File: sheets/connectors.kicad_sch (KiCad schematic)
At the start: 4 parts

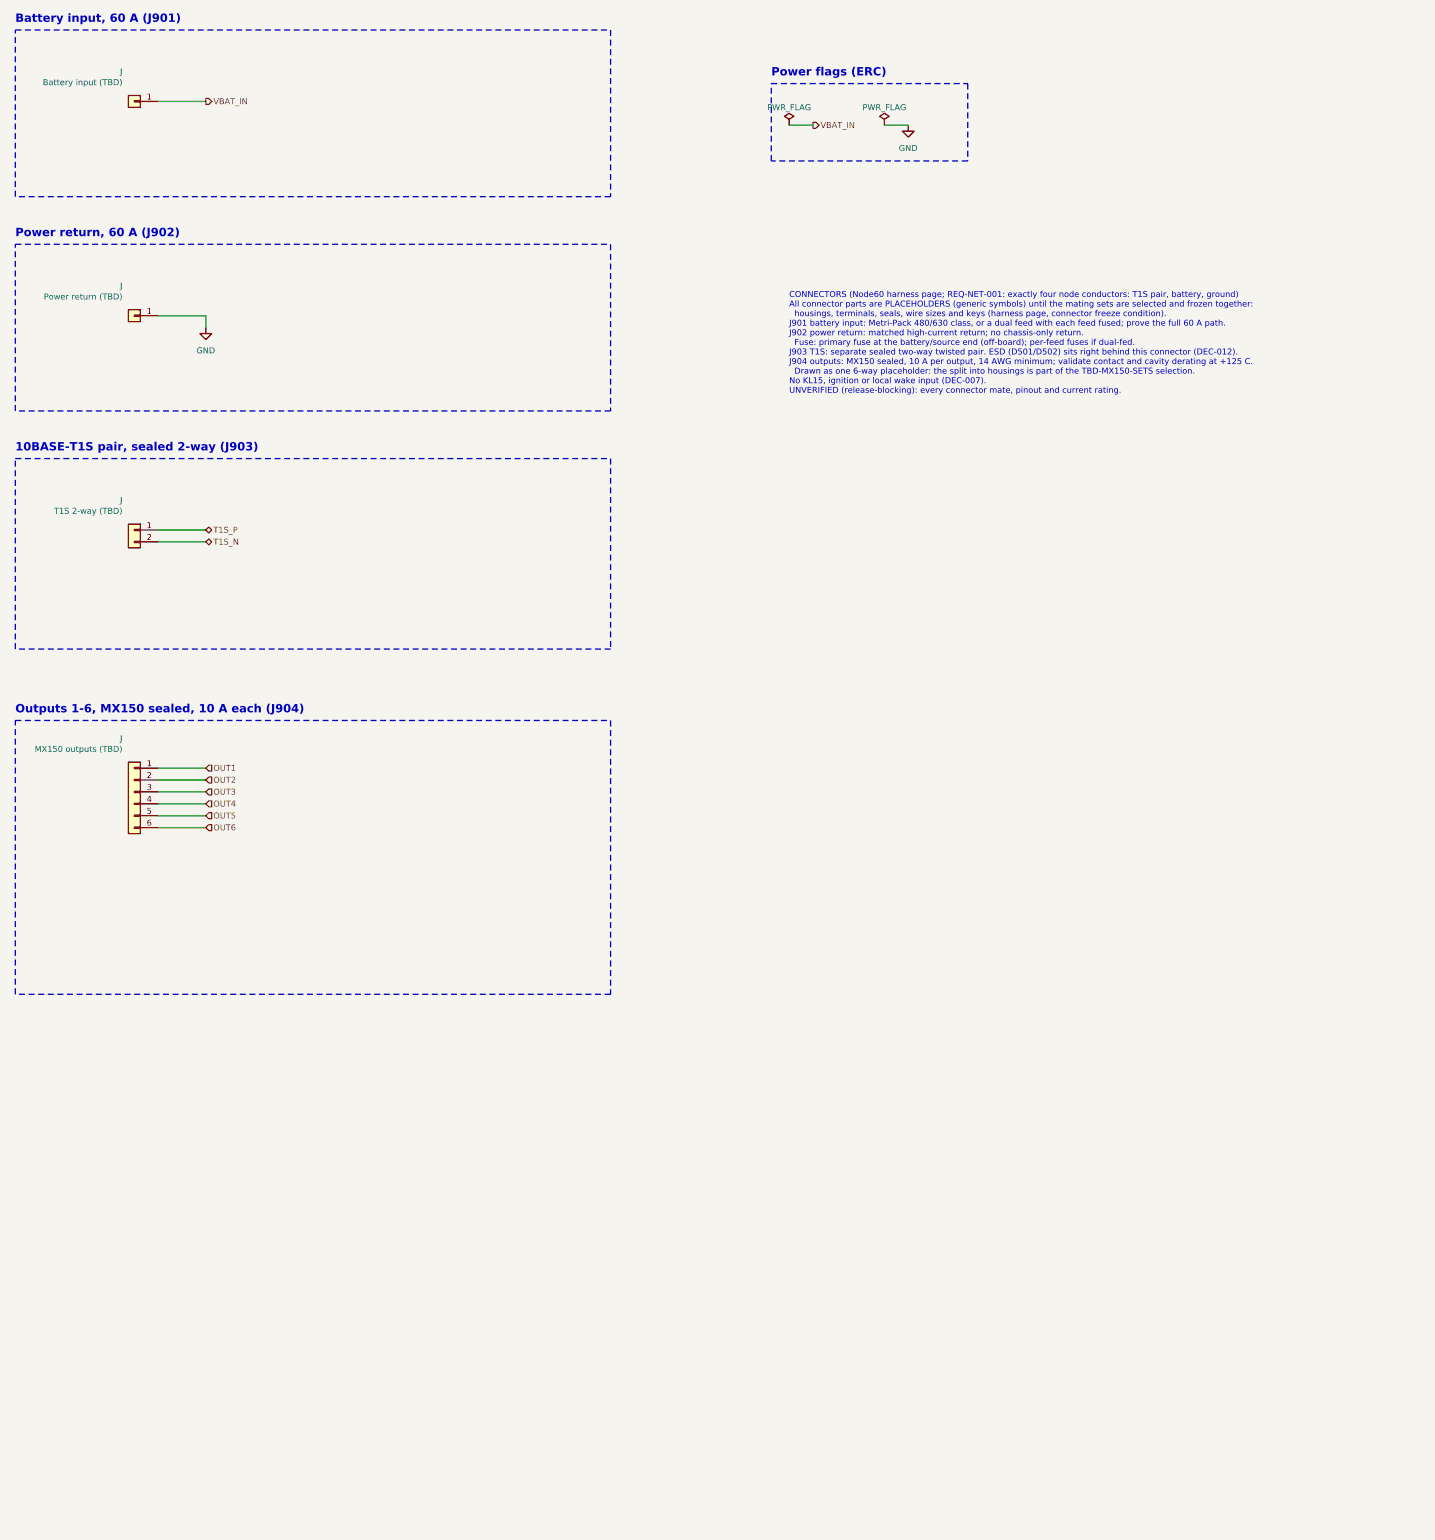
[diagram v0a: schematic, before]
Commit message: Connectors: six DT13-2P output headers replace the MX150 placeholder
J904-J909, one TE Deutsch DT13-2P per output (DEC-013, node60-hw PR #8).
Still placeholders until DropOut_Connector:DT13-2P lands (library PR
#19). Pin 1 carries OUTx; pin 2 stays unconnected with a visible note
until the pin assignment (local ground return vs paralleled output) is
decided.

Co-Authored-By: Claude Opus 5.5 <noreply@anthropic.com>
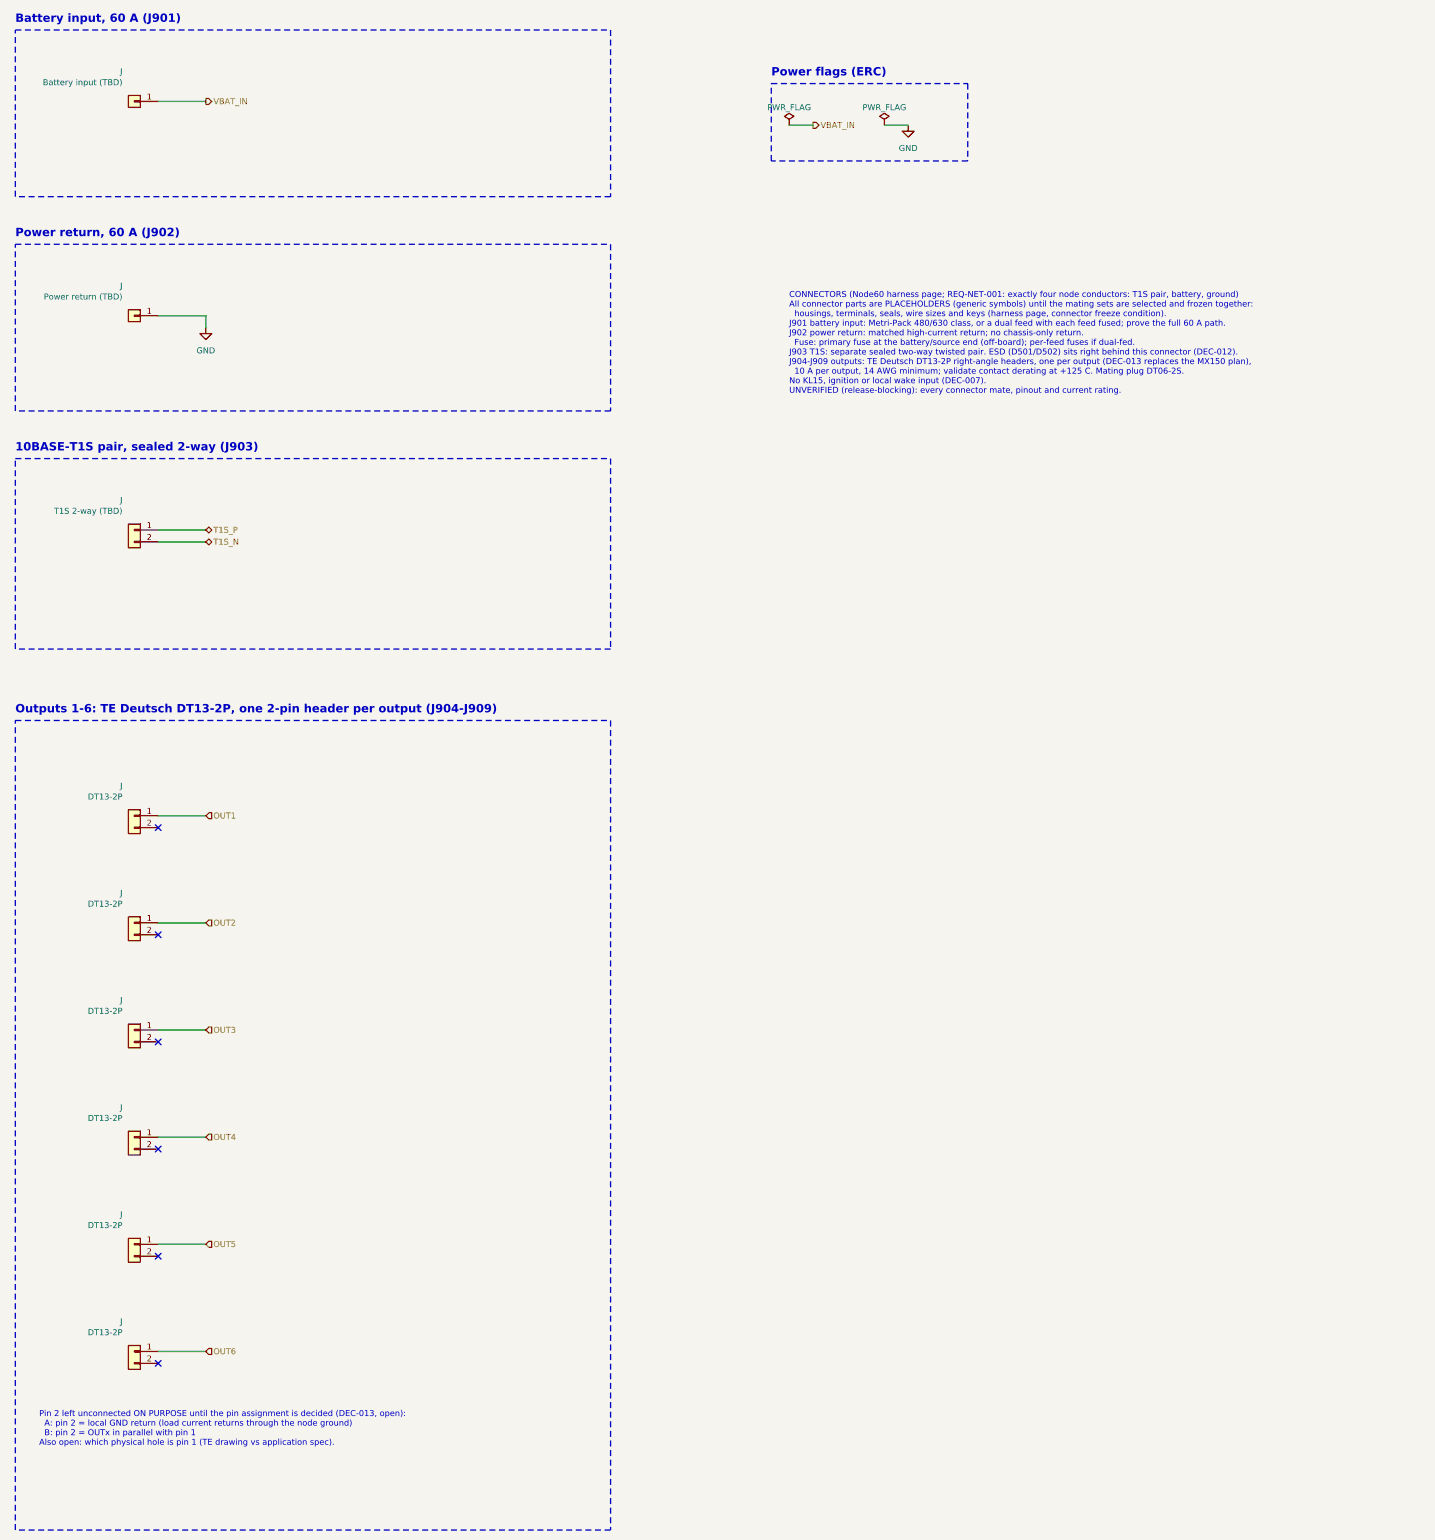
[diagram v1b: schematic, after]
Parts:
- added J (x5): DT13-2P, symbol Connector_Generic:Conn_01x02
- J: value MX150 outputs (TBD) -> DT13-2P; symbol Connector_Generic:Conn_01x06 -> Connector_Generic:Conn_01x02; Placeholder PLACEHOLDER: TBD part: selection pending user decision (fin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 -> PLACEHOLDER: selected 2026-10-23 (DEC-013): TE DT13-2P; lib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
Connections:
- net OUT2: now also J.1 (Pin_1); no longer J.2 (Pin_2)
- net OUT3: now also J.1 (Pin_1); no longer J.3 (Pin_3)
- net OUT4: now also J.1 (Pin_1); no longer J.4 (Pin_4)
- net OUT5: now also J.1 (Pin_1); no longer J.5 (Pin_5)
- net OUT6: now also J.1 (Pin_1); no longer J.6 (Pin_6)
- no-connect marks 0 -> 6
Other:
- note added: "Outputs 1-6: TE Deutsch DT13-2P, one 2-pin header per output (J904-J909)"
- note added: "Pin 2 left unconnected ON PURPOSE until the pin assignment is decided (DEC-013, open): A: pin 2 = local GND return (load current returns through the node ground) B: pin 2 = OUTx in parallel with pin 1 Also open: which physical hole is pin 1 (TE drawing vs application spec)."
- note removed: "Outputs 1-6, MX150 sealed, 10 A each (J904)"

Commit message: Connectors: DT13-2P pin 2 is the load ground return
Per DEC-013 (decided 2026-10-22, node60-hw PR #8): pin 1 = OUTx, pin 2 =
that load's ground return, on the single GND net. The sheet notes the
layout consequences: each return sized like its 10 A output and routed
to the power-entry star region, never across the logic ground, with up
to 60 A of load return leaving through J902.

Co-Authored-By: Claude Opus 5.5 <noreply@anthropic.com>
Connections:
- net GND: now also J.2 (Pin_2), J.2 (Pin_2), J.2 (Pin_2), J.2 (Pin_2), J.2 (Pin_2), J.2 (Pin_2)
- no-connect marks 6 -> 0
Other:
- note added: "Pin 1 = OUTx, pin 2 = that load's ground return (DEC-013, decided 2026-10-22). LAYOUT: each pin 2 return carries up to 10 A, like its OUTx: same copper and via treatment. Route pin 2 returns to the power-entry ground star region, never across the logic ground. Up to 60 A of load return flows from the headers to the star region and out through J902. RELEASE-BLOCKING: which physical hole is pin 1 (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"
- note removed: "Pin 2 left unconnected ON PURPOSE until the pin assignment is decided (DEC-013, open): A: pin 2 = local GND return (load current returns through the node ground) B: pin 2 = OUTx in parallel with pin 1 Also open: which physical hole is pin 1 (TE drawing vs application spec)."

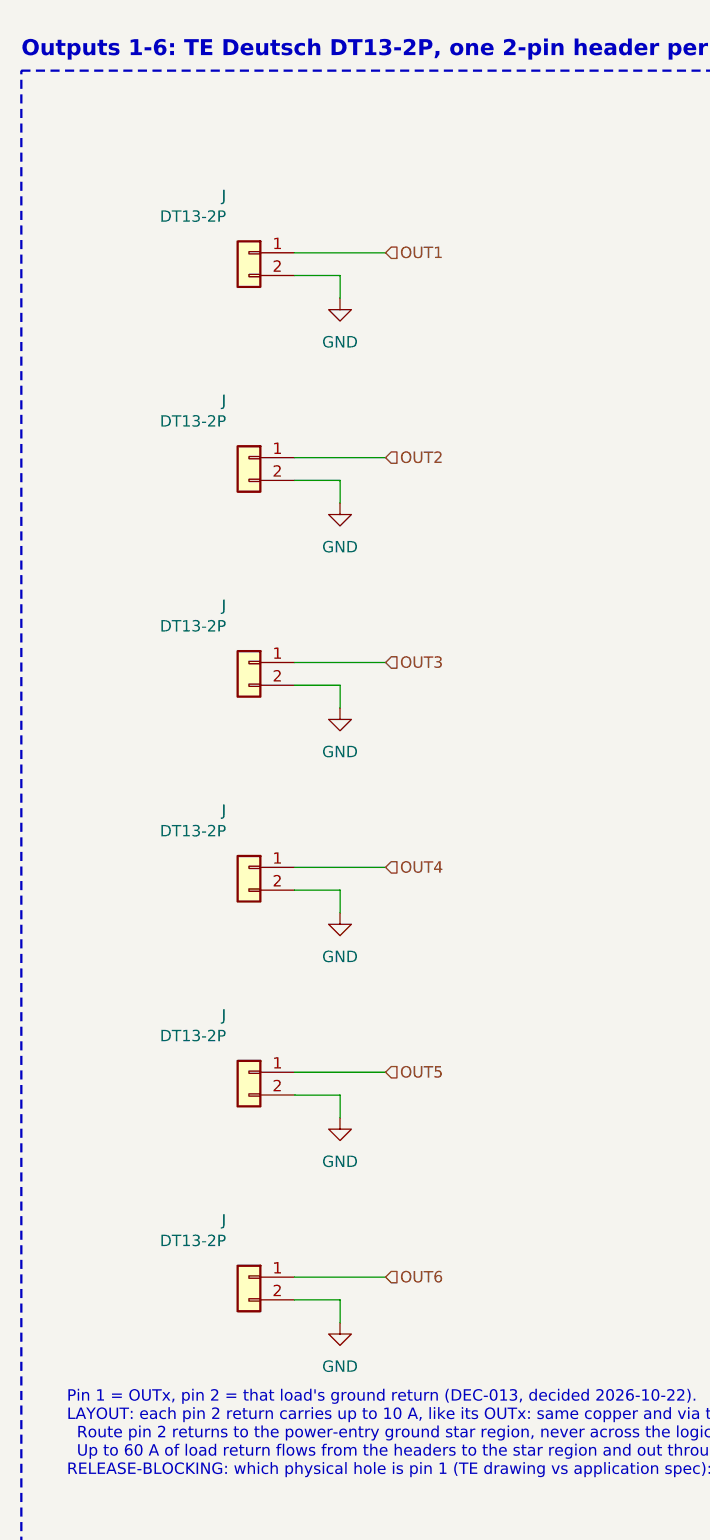
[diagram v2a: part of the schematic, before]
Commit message: Swap placeholders for merged DropOut library parts
Library bumped to ce98ecf (PRs #15, #16, #18, #19, #20, #21 merged).
Now real parts: IAUTN08S5N012LATMA1 (Q201-Q204, dual gate: G_ON and
G_LIN both driven), CSS2725FTL250 (R201, 2-terminal: sense nets are
VBAT_D / VBAT_Q2D with Kelvin taps from the pads in layout),
TPS7B8133QWDRVRQ1 (U301, COUT 2.2uF per its 1-200 uF requirement),
NCU18XH103F6SRB (RT201, RT601-801), Wurth 74438356022HT / 74438356010HT
buck inductors and Harwin S1751-46R GND loops (user's picks 2026-10-23),
1 mm pad test points and DT13-2P output headers. The library pin-type
fixes cut the ERC exclusions from 17 to 2. parts.yaml records the
library symbols; the library tables list the new libraries.

Co-Authored-By: Claude Opus 5.5 <noreply@anthropic.com>
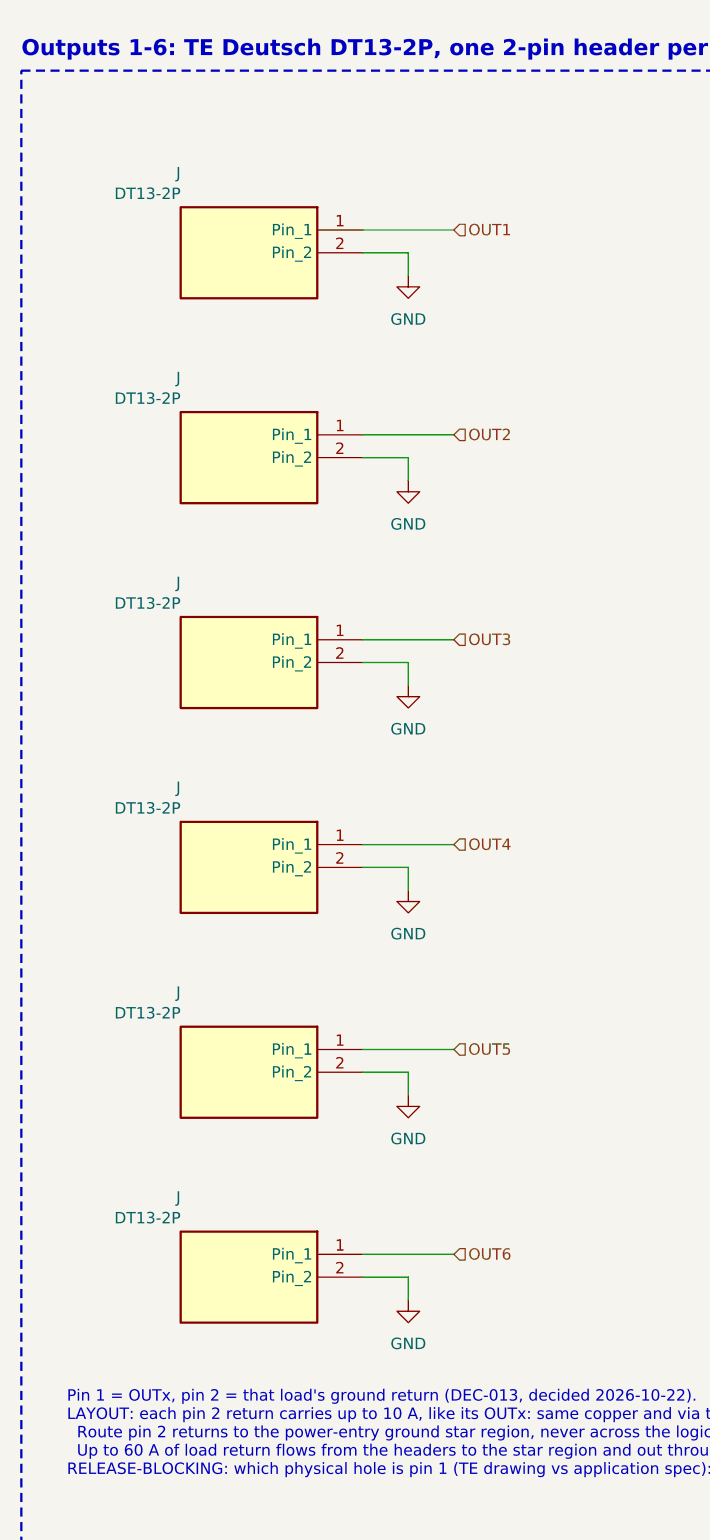
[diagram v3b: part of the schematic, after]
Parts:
- J: footprint (none) -> DropOut_Connector_TE-Connectivity:TE_DEUTSCH-DT_DT13-2P_1x02_P5.46mm_Horizontal; symbol Connector_Generic:Conn_01x02 -> DropOut_Connector:DT13-2P; DigiKey_PN (none) -> 1734-1452-ND; MPN (none) -> DT13-2P; Manufacturer (none) -> TE Connectivity; Mouser_PN (none) -> 571-DT13-2P; Notes (none) -> Mates DT06-2S + W2S wedgelock. No current derating curve; +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; Placeholder PLACEHOLDER: selected 2026-10-23 (DEC-013): TE DT13-2P; lib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 -> (none); Temperature_Grade (none) -> -55 to +125 °C (not AEC qualified)
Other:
- moved on the sheet: J
